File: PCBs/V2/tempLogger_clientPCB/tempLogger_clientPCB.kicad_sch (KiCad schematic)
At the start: 5 parts

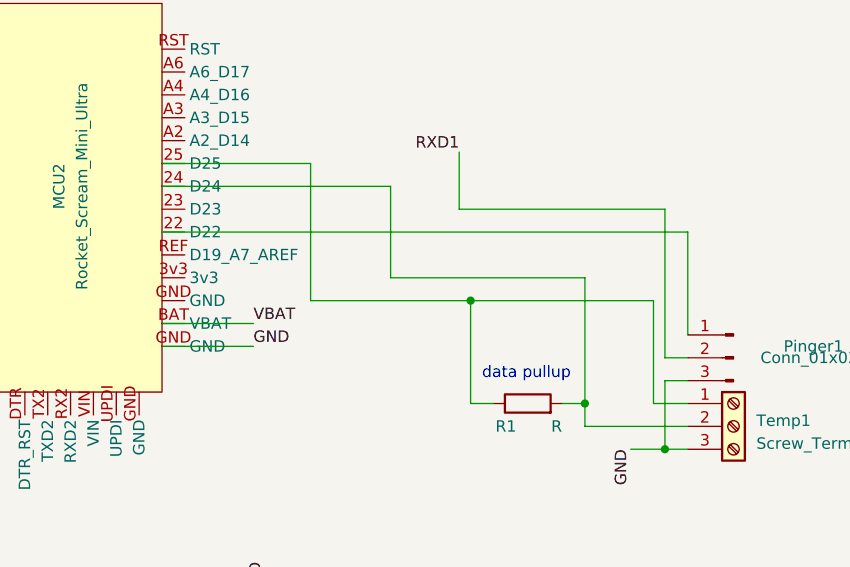
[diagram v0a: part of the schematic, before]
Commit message: fixed packetIndex ISR bug in TC code. added state 0.
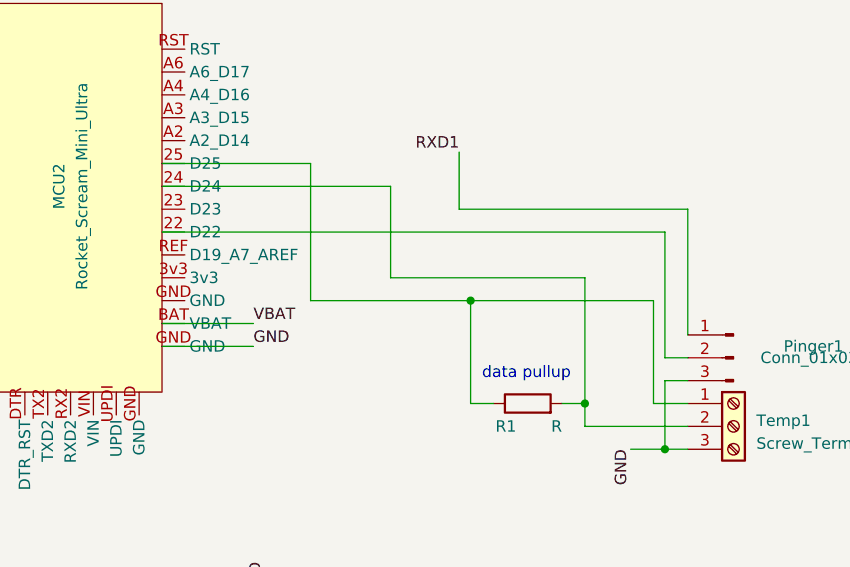
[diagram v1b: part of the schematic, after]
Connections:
- net RXD1: now also Pinger1.1 (Pin_1); no longer Pinger1.2 (Pin_2)
- net at MCU2.22 (D22): now also Pinger1.2 (Pin_2); no longer Pinger1.1 (Pin_1)
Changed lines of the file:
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@@
   (junction (at 160.02 85.09) (diameter 0) (color 0 0 0 0)
   )
-  (wire (pts (xy 171.45 66.04) (xy 171.45 77.47))
+  (wire (pts (xy 124.46 106.68) (xy 124.46 110.49))
     (stroke (width 0) (type default))
   )
-  (wire (pts (xy 168.91 63.5) (xy 168.91 80.01))
-    (stroke (width 0) (type default))
-  )
-  (wire (pts (xy 124.46 106.68) (xy 124.46 110.49))
+  (wire (pts (xy 146.05 63.5) (xy 171.45 63.5))
     (stroke (width 0) (type default))
   )
@@
     (stroke (width 0) (type default))
   )
-  (wire (pts (xy 146.05 63.5) (xy 168.91 63.5))
+  (wire (pts (xy 168.91 66.04) (xy 168.91 80.01))
     (stroke (width 0) (type default))
   )
@@
     (stroke (width 0) (type default))
   )
+  (wire (pts (xy 168.91 66.04) (xy 113.03 66.04))
+    (stroke (width 0) (type default))
+  )
   (wire (pts (xy 129.54 73.66) (xy 147.32 73.66))
     (stroke (width 0) (type default))
@@
     (stroke (width 0) (type default))
   )
-  (wire (pts (xy 171.45 66.04) (xy 113.03 66.04))
+  (wire (pts (xy 171.45 63.5) (xy 171.45 77.47))
     (stroke (width 0) (type default))
   )
